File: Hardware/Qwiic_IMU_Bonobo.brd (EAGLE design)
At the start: 30.5 x 25.4 mm, 89 parts, among them J2 SMD, J3 PTH, J4 SMD, J6 SPI, U2 BNO080, Y1 32.768kHz

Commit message: Silk updated to BNO086 and vectors
-Product name silk updated to BNO086
-all silk updated to vector buzzard style
-Jumpers updated to newest packages
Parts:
- removed SJ2: (no value), SparkFun:SJ_2S-NO
- removed U$26: (no value), buzzard_labels (2):#INT0
- removed U$28: (no value), buzzard_labels (2):PS14
- removed U$59: (no value), Qwiic#Label#Full#M#png (6):QWIIC#LABEL#FULL#M#PNG
- added ADR: (no value), SparkFun-Jumpers:SMT-JUMPER_2_NO_SILK
- added U$24: (no value), output:BNO0861
- added U$31: (no value), output:IMU862
- added U$32, U$45: (no value), output:#GND#864
- added U$36: (no value), output:#3V3#865
- added U$37: (no value), output:#SCK#866
- added U$38: (no value), output:##WAK##871
- added U$48: (no value), output:#SCL#875
- added U$56: (no value), output:#SI#884
- added U$57: (no value), output:#PS0#895
- SJ1: value (none) -> JUMPER-SMT_3_2-NC_PASTE_SILK
- SJ3, SJ4: device SparkFun:SJ_2S-NO -> SparkFun-Jumpers:SMT-JUMPER_2_NO_SILK
- U$1: device Labels-0_04:(PWR) -> output:#I2C#874
- U$10: device Labels-0_04:3V3 -> output:Y879
- U$11: device buzzard_labels (4):3V30 -> output:#SCK#882
- U$12: device buzzard_labels (6):SCK0 -> output:#SO#867
- U$13: device buzzard_labels (6):SCK0 -> output:#SI#868
- U$14: device buzzard_labels (8):PS03 -> output:#SDA#3
- U$15: device Labels-0_04:GND -> output:Z880
- U$16: device Labels-0_04:GND -> output:#GND#2
- U$17: device buzzard_labels (7):SI1 -> output:##CS##870
- U$18: device buzzard_labels (7):SI1 -> output:##CS##885
- U$19: device buzzard_labels (5):#WAK6 -> output:##RST##872
- U$2: device buzzard_labels (11):BOOT2 -> output:BLK889
- U$20: device buzzard_labels (5):#WAK6 -> output:##RST##887
- U$21: device buzzard_labels (8):3V32 -> output:RXI891
- U$22: device buzzard_labels (8):RXI1 -> output:TXO892
- U$23: device Labels-0_04:(I_SUPER2_C) -> output:#PS0#874
- U$25: device buzzard_labels (2):#INT0 -> output:X878
- U$27: device buzzard_labels (2):PS14 -> output:#3V3#874
- U$29: device buzzard_labels (2):PS05 -> SparkFun-Aesthetics:QWIIC_4MM
- U$3: device Labels-0_04:#RST> -> output:X878
- U$30: device buzzard_labels (9):ADR0 -> output:#ADR#894
- U$33: device buzzard_labels (2):PS114 -> output:#PS1#1
- U$34: device buzzard_labels (2):PS015 -> output:#PS0#2
- U$35: device buzzard_labels (8):TXO0 -> output:#PS1#895
- U$39: device buzzard_labels (2):UART8 -> output:#3V3#882
- U$4: device Labels-0_04:#RST> -> output:##INT##6
- U$40: device buzzard_labels (2):GRN10 -> output:3V3891
- U$41: device buzzard_labels (2):BLK9 -> output:GRN890
- U$42: device buzzard_labels (5):GND1 -> output:#PWR#873
- U$43: device buzzard_labels (5):GND1 -> output:#PS1#874
- U$44: device buzzard_labels (2):BNO080_IMU11 -> output:UART881
- U$46: device buzzard_labels (2):BNO08012 -> output:#3V3#874
- U$47: device buzzard_labels (2):IMU13 -> output:#SDA#874
- U$49: device buzzard_labels (5):#RST7 -> output:#BOOT#888
- U$5: device Labels-0_04:SCL -> output:##RST##5
- U$50: device buzzard_labels (4):3V30 -> output:##RST##876
- U$51: device buzzard_labels (5):#RST7 -> output:##INT##877
- U$52: device buzzard_labels (6):#CS3 -> SparkFun-Aesthetics:QWIIC_6MM
- U$53: device buzzard_labels (6):#CS3 -> output:##WAK##886
- U$54: device buzzard_labels (7):SO0 -> output:BNO086_IMU881
- U$55: device buzzard_labels (7):SO0 -> output:#SO#883
- U$6: device Labels-0_04:SCL -> output:Y879
- U$7: device Labels-0_04:SDA -> output:Z880
- U$8: device Labels-0_04:SDA -> output:#SCL#4
- U$9: device Labels-0_04:3V3 -> output:#GND#2
- moved U$6 25.4 mm to (1.86, 20.3), turned to 0 degrees
- moved U$25 25.2 mm to (4.36, 17.1), flipped to the bottom, turned to 0 degrees
- moved U$49 24.8 mm to (1.24, 10.4)
- moved U$3 23.1 mm to (4.51, 17.1), turned to 0 degrees
- moved U$23 22.5 mm to (6.37, 3.56)
- moved U$10 22.3 mm to (1.70, 20.3), flipped to the bottom, turned to 0 degrees
- moved U$7 21.4 mm to (5.02, 19.7), turned to 0 degrees
- moved U$39 20.9 mm to (8.88, 21.7), turned to 90 degrees
- moved U$16 20.7 mm to (6.37, 21.7)
- moved U$50 20.3 mm to (21.6, 3.66)
- moved U$42 20.1 mm to (26.4, 18.2), flipped to the top
- moved U$15 19.1 mm to (4.97, 19.7), flipped to the bottom, turned to 0 degrees
- moved U$51 16.4 mm to (24.1, 3.54)
- moved U$43 16.2 mm to (8.89, 3.47)
- moved U$35 16.1 mm to (3.92, 8.89), turned to 0 degrees
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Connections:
- net ADDR/MOSI: now also ADR.2; no longer SJ2.2
- net GND: now also ADR.1; no longer SJ2.1
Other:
- board text removed: "X"
- board text removed: "Y"
- board text removed: "Z"

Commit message: Ordering instructions added
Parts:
- added U$59: (no value), SparkFun-Aesthetics:ORDERING_INSTRUCTIONS
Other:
- board text added: "Soldermask: Red Thickness: 1.6mm 2-Layer Design 1oz copper Finish: HASL"
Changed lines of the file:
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@@
 <layer number="45" name="Holes" color="7" fill="1" visible="yes" active="yes"/>
 <layer number="46" name="Milling" color="3" fill="1" visible="no" active="yes"/>
-<layer number="47" name="Measures" color="7" fill="1" visible="no" active="yes"/>
+<layer number="47" name="Measures" color="7" fill="1" visible="yes" active="yes"/>
 <layer number="48" name="Document" color="7" fill="1" visible="no" active="yes"/>
 <layer number="49" name="Reference" color="7" fill="1" visible="yes" active="yes"/>
@@
 <text x="17.78" y="-10.16" size="1.778" layer="51" font="vector">A. England</text>
 <dimension x1="0" y1="25.4" x2="30.48" y2="25.4" x3="15.24" y3="35.56" textsize="1.27" layer="47" unit="inch"/>
+<text x="47.498" y="44.069" size="1.778" layer="51" font="vector" align="top-left">Soldermask: Red
+Thickness: 1.6mm
+2-Layer Design
+1oz copper
+Finish: HASL</text>
 </plain>
 <attributes>
@@
 <element name="U$4" library="output" package="##INT##6" value="" x="24.102059375" y="3.4544" smashed="yes" rot="MR90"/>
 <element name="U$16" library="output" package="#GND#2" value="" x="6.37031875" y="21.7271625" smashed="yes" rot="MR90"/>
+<element name="U$59" library="SparkFun-Aesthetics" package="ORDERING_INSTRUCTIONS" value="" x="45.72" y="54.61" smashed="yes"/>
 </elements>
 <signals>
@@
 </drawing>
 <compatibility>
+<note version="6.3" minversion="6.2.2" severity="warning">
+Since Version 6.2.2 text objects can contain more than one line,
+which will not be processed correctly with this version.
+</note>
 <note version="8.3" severity="warning">
 Since Version 8.3, EAGLE supports URNs for individual library

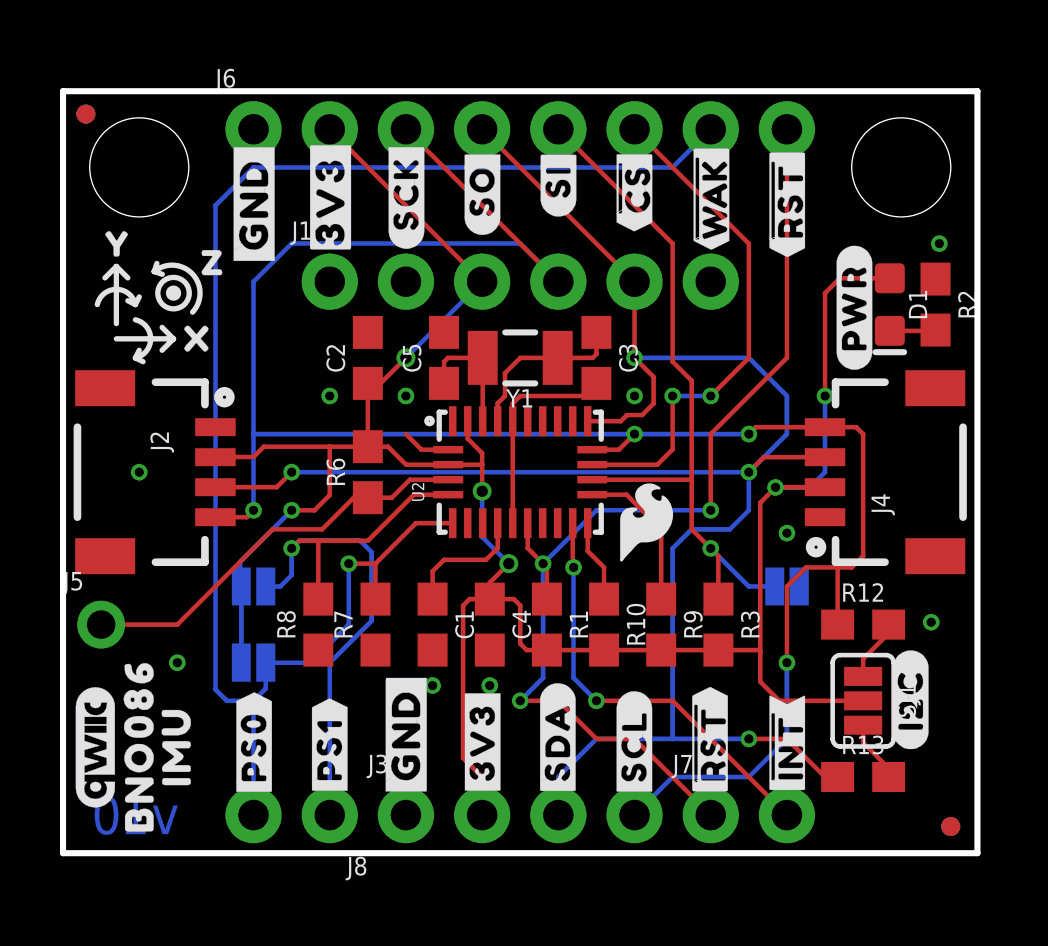
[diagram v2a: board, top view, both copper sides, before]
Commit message: minor stuff - measures, library work
-added measures and units
-replaced some connectors, fids, standoffs, GND symbols to newer libraries.
-renamed jumpers (in SCH) to match silk names (on board).
-Red LED to new King Bright version, also updated resistor value to 4.7K
-some minor schematic cleanup
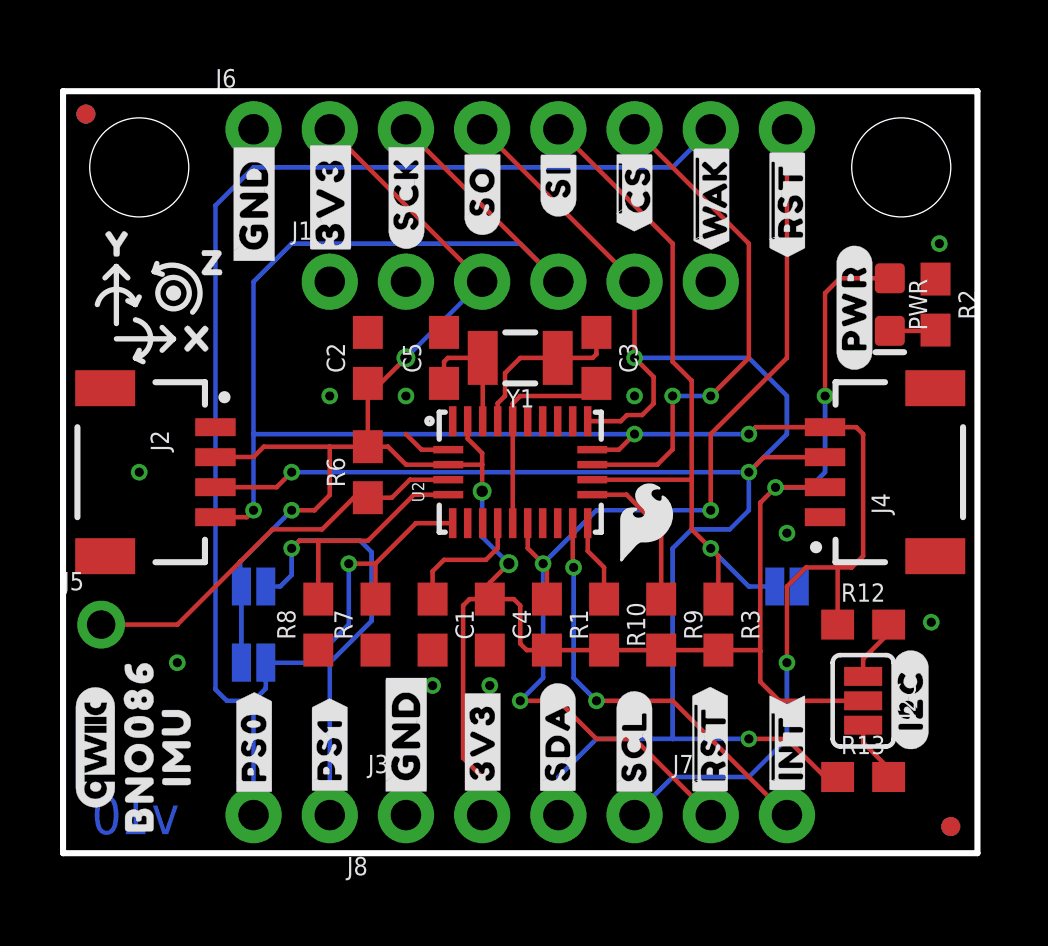
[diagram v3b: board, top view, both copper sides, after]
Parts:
- I2C: value JUMPER-SMT_3_2-NC_PASTE_SILK -> (none)
- J2, J4: device SparkX:1X04_1MM_RA -> SparkFun-Connectors:JST04_1MM_RA
- J3: device SparkX:1X04_NO_SILK -> SparkFun-Connectors:1X04_NO_SILK
- JP1, JP2, JP5, JP6: device SparkFun:MICRO-FIDUCIAL -> SparkFun-Aesthetics:FIDUCIAL-MICRO
- JP3, JP4: device SparkFun:STAND-OFF -> SparkFun-Hardware:STAND-OFF
- R2: value 1k -> 4.7k
- renumbered D1 to PWR, SJ1 to I2C, SJ3 to PS0, SJ4 to PS1
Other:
- board text added: "Measure Units: INCHES"
